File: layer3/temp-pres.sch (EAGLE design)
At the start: 9 parts, among them U1 TMP1021:1, U2 MS5803-14BA

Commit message: intital board layout
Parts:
- C1: device SparkFun:CAP0603-CAP -> microbuilder:CAP_CERAMIC0805-NOOUTLINE
- C2: device SparkFun-Capacitors:0.1UF-25V(+80/-20%)(0603) -> microbuilder:CAP_CERAMIC0805-NOOUTLINE
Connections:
- removed net ALERT: R3.2
- new net N$1: R3.2, U1.ALERT
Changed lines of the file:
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@@
 </classes>
 <parts>
-<part name="C1" library="SparkFun" deviceset="CAP" device="0603-CAP" value="0.1uF"/>
 <part name="U1" library="SparkFun-Sensors" deviceset="TMP102" device="1:1"/>
 <part name="U2" library="MS5803" deviceset="MS5803-14BA" device=""/>
-<part name="C2" library="SparkFun-Capacitors" deviceset="0.1UF-25V(+80/-20%)(0603)" device="" value="0.1uF"/>
 <part name="GND1" library="SparkFun-Aesthetics" deviceset="GND" device=""/>
 <part name="J1" library="SparkFun-Connectors" deviceset="M04" device="PTH"/>
@@
 <part name="R4" library="microbuilder" deviceset="RESISTOR" device="_0805MP" value="10K"/>
 <part name="GND2" library="SparkFun-Aesthetics" deviceset="GND" device=""/>
+<part name="C1" library="microbuilder" deviceset="CAP_CERAMIC" device="0805-NOOUTLINE" value="0.1uF"/>
+<part name="C2" library="microbuilder" deviceset="CAP_CERAMIC" device="0805-NOOUTLINE" value="0.1uF"/>
 </parts>
 <sheets>
@@
 </plain>
 <instances>
-<instance part="C1" gate="G$1" x="7.62" y="71.12"/>
 <instance part="U1" gate="G$1" x="27.94" y="27.94"/>
 <instance part="U2" gate="G$1" x="104.14" y="71.12"/>
-<instance part="C2" gate="G$1" x="20.32" y="71.12"/>
 <instance part="GND1" gate="1" x="20.32" y="63.5"/>
 <instance part="J1" gate="G$1" x="55.88" y="68.58"/>
@@
 <instance part="R4" gate="G$1" x="132.08" y="91.44" rot="R270"/>
 <instance part="GND2" gate="1" x="7.62" y="63.5"/>
+<instance part="C1" gate="G$1" x="7.62" y="71.12"/>
+<instance part="C2" gate="G$1" x="20.32" y="71.12"/>
 </instances>
 <busses>
@@
 <net name="GND" class="0">
 <segment>
-<pinref part="C2" gate="G$1" pin="2"/>
 <pinref part="GND1" gate="1" pin="GND"/>
 <wire x1="20.32" y1="66.04" x2="20.32" y2="68.58" width="0.1524" layer="91"/>
+<pinref part="C2" gate="G$1" pin="2"/>
 </segment>
 <segment>
@@
 <segment>
 <pinref part="GND2" gate="1" pin="GND"/>
+<wire x1="7.62" y1="66.04" x2="7.62" y2="68.58" width="0.1524" layer="91"/>
 <pinref part="C1" gate="G$1" pin="2"/>
-<wire x1="7.62" y1="66.04" x2="7.62" y2="68.58" width="0.1524" layer="91"/>
 </segment>
 <segment>
@@
 <wire x1="38.1" y1="30.48" x2="45.72" y2="30.48" width="0.1524" layer="91"/>
 <label x="45.72" y="30.48" size="1.27" layer="95" xref="yes"/>
-</segment>
-</net>
-<net name="ALERT" class="0">
-<segment>
-<wire x1="38.1" y1="25.4" x2="55.88" y2="25.4" width="0.1524" layer="91"/>
-<label x="40.64" y="25.4" size="1.27" layer="95"/>
-<pinref part="R3" gate="G$1" pin="2"/>
 </segment>
 </net>
@@
 <net name="+3V3" class="0">
 <segment>
-<pinref part="C2" gate="G$1" pin="1"/>
 <wire x1="20.32" y1="78.74" x2="20.32" y2="76.2" width="0.1524" layer="91"/>
 <label x="20.32" y="78.74" size="1.27" layer="95" rot="R90" xref="yes"/>
+<pinref part="C2" gate="G$1" pin="1"/>
 </segment>
 <segment>
@@
 </segment>
 <segment>
-<pinref part="C1" gate="G$1" pin="1"/>
 <wire x1="7.62" y1="78.74" x2="7.62" y2="76.2" width="0.1524" layer="91"/>
 <label x="7.62" y="78.74" size="1.27" layer="95" rot="R90" xref="yes"/>
+<pinref part="C1" gate="G$1" pin="1"/>
 </segment>
 <segment>
@@
 </segment>
 </net>
+<net name="N$1" class="0">
+<segment>
+<pinref part="U1" gate="G$1" pin="ALERT"/>
+<pinref part="R3" gate="G$1" pin="2"/>
+<wire x1="38.1" y1="25.4" x2="55.88" y2="25.4" width="0.1524" layer="91"/>
+</segment>
+</net>

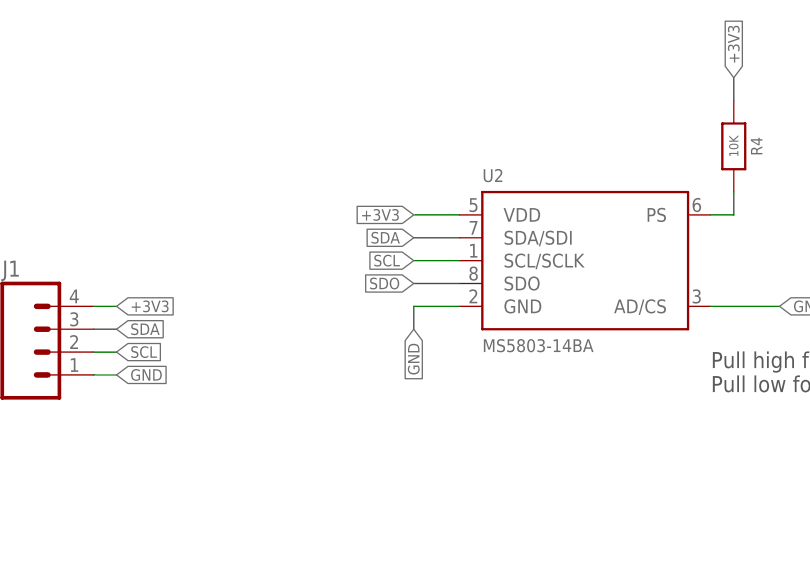
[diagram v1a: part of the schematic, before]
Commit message: removed serial data output (SDO) from schematic bc it is not needed. Since it is an output I blieve it is safe to let it float.
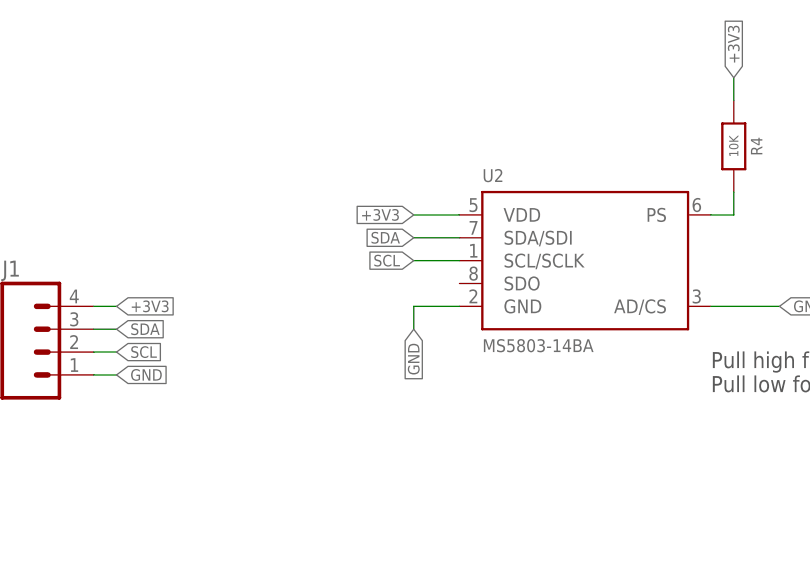
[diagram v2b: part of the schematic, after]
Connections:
- removed net SDO: U2.SDO
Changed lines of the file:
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@@
 <setting verticaltext="up"/>
 </settings>
-<grid distance="0.1" unitdist="inch" unit="inch" style="lines" multiple="1" display="yes" altdistance="0.01" altunitdist="inch" altunit="inch"/>
+<grid distance="0.1" unitdist="inch" unit="inch" style="lines" multiple="1" display="no" altdistance="0.01" altunitdist="inch" altunit="inch"/>
 <layers>
 <layer number="1" name="Top" color="4" fill="1" visible="no" active="no"/>
@@
 </segment>
 </net>
-<net name="SDO" class="0">
-<segment>
-<pinref part="U2" gate="G$1" pin="SDO"/>
-<wire x1="101.6" y1="76.2" x2="96.52" y2="76.2" width="0.1524" layer="91"/>
-<label x="96.52" y="76.2" size="1.27" layer="95" rot="R180" xref="yes"/>
-</segment>
-</net>

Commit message: calrified commints
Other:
- note added: "10010010 (0x92) when ADD0 to VCC. 10010000 (0x90) when ADD0 to GND."
- note removed: "10010010 (0x92) when jumpered to VCC. 10010000 (0x90) when jumpered to GND. (default)"
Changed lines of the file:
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@@
 <sheet>
 <plain>
-<text x="39.116" y="12.192" size="1.778" layer="97">10010010 (0x92) when jumpered to VCC.
-10010000 (0x90) when jumpered to GND. (default)</text>
+<text x="39.116" y="12.192" size="1.778" layer="97">10010010 (0x92) when ADD0 to VCC.
+10010000 (0x90) when ADD0 to GND. </text>
 <text x="129.54" y="68.58" size="1.778" layer="97" align="top-left">Pull high for 0x76.
 Pull low for 0x77

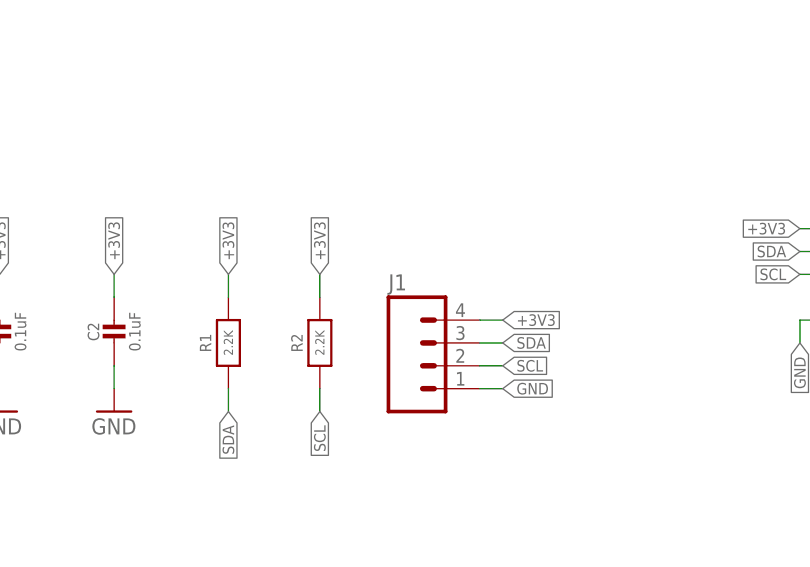
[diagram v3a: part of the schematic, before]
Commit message: tweaked layer3 silk screen for printing
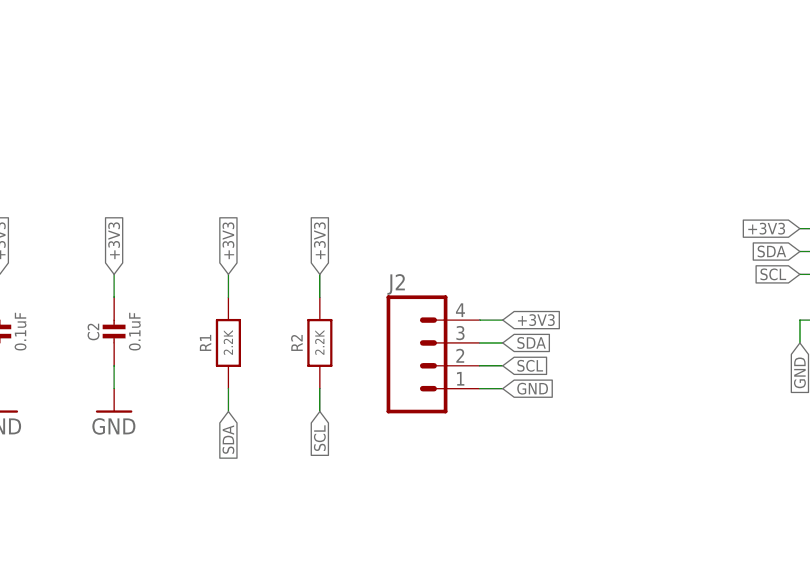
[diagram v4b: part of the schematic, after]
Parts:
- removed J1: (no value), SparkFun-Connectors:M04PTH
- added J2: (no value), SparkFun-Connectors:M04NO_SILK_ALL_ROUND
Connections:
- net +3V3: now also J2.4; no longer J1.4
- net GND: now also J2.1; no longer J1.1
- net SCL: now also J2.2; no longer J1.2
- net SDA: now also J2.3; no longer J1.3
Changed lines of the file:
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@@
 <part name="U2" library="MS5803" deviceset="MS5803-14BA" device=""/>
 <part name="GND1" library="SparkFun-Aesthetics" deviceset="GND" device=""/>
-<part name="J1" library="SparkFun-Connectors" deviceset="M04" device="PTH"/>
 <part name="R1" library="microbuilder" deviceset="RESISTOR" device="_0805MP" value="2.2K"/>
 <part name="R2" library="microbuilder" deviceset="RESISTOR" device="_0805MP" value="2.2K"/>
@@
 <part name="C1" library="microbuilder" deviceset="CAP_CERAMIC" device="0805-NOOUTLINE" value="0.1uF"/>
 <part name="C2" library="microbuilder" deviceset="CAP_CERAMIC" device="0805-NOOUTLINE" value="0.1uF"/>
+<part name="J2" library="SparkFun-Connectors" deviceset="M04" device="NO_SILK_ALL_ROUND"/>
 </parts>
 <sheets>
@@
 <instance part="U2" gate="G$1" x="104.14" y="71.12"/>
 <instance part="GND1" gate="1" x="20.32" y="63.5"/>
-<instance part="J1" gate="G$1" x="55.88" y="68.58"/>
 <instance part="R1" gate="G$1" x="33.02" y="71.12" rot="R90"/>
 <instance part="R2" gate="G$1" x="43.18" y="71.12" rot="R90"/>
@@
 <instance part="C1" gate="G$1" x="7.62" y="71.12"/>
 <instance part="C2" gate="G$1" x="20.32" y="71.12"/>
+<instance part="J2" gate="G$1" x="55.88" y="68.58"/>
 </instances>
 <busses>
@@
 </segment>
 <segment>
-<pinref part="J1" gate="G$1" pin="1"/>
 <wire x1="60.96" y1="66.04" x2="63.5" y2="66.04" width="0.1524" layer="91"/>
 <label x="63.5" y="66.04" size="1.27" layer="95" xref="yes"/>
+<pinref part="J2" gate="G$1" pin="1"/>
 </segment>
 <segment>
@@
 </segment>
 <segment>
-<pinref part="J1" gate="G$1" pin="2"/>
 <wire x1="60.96" y1="68.58" x2="63.5" y2="68.58" width="0.1524" layer="91"/>
 <label x="63.5" y="68.58" size="1.27" layer="95" xref="yes"/>
+<pinref part="J2" gate="G$1" pin="2"/>
 </segment>
 <segment>
@@
 </segment>
 <segment>
-<pinref part="J1" gate="G$1" pin="3"/>
 <wire x1="60.96" y1="71.12" x2="63.5" y2="71.12" width="0.1524" layer="91"/>
 <label x="63.5" y="71.12" size="1.27" layer="95" xref="yes"/>
+<pinref part="J2" gate="G$1" pin="3"/>
 </segment>
 <segment>
@@
 </segment>
 <segment>
-<pinref part="J1" gate="G$1" pin="4"/>
 <wire x1="60.96" y1="73.66" x2="63.5" y2="73.66" width="0.1524" layer="91"/>
 <label x="63.5" y="73.66" size="1.27" layer="95" xref="yes"/>
+<pinref part="J2" gate="G$1" pin="4"/>
 </segment>
 </net>
